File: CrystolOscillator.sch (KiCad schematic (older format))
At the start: 4 parts, among them Y501 32.768kHz, Y502 48MHz

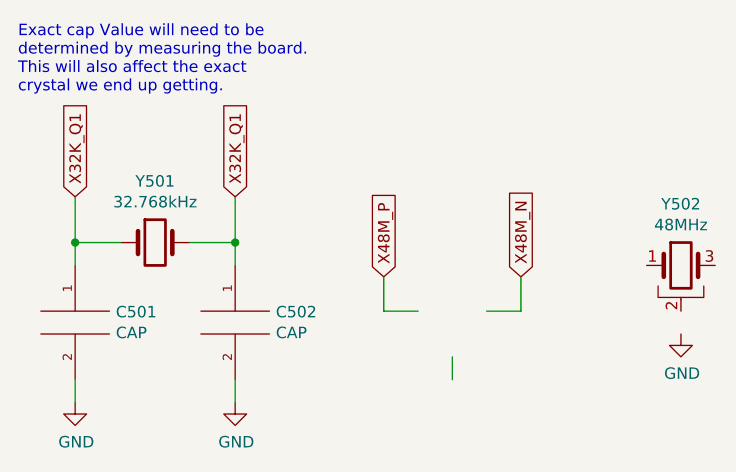
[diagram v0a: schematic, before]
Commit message: fixed the 20dBm branch and switched back to the 3 port band switcher IC
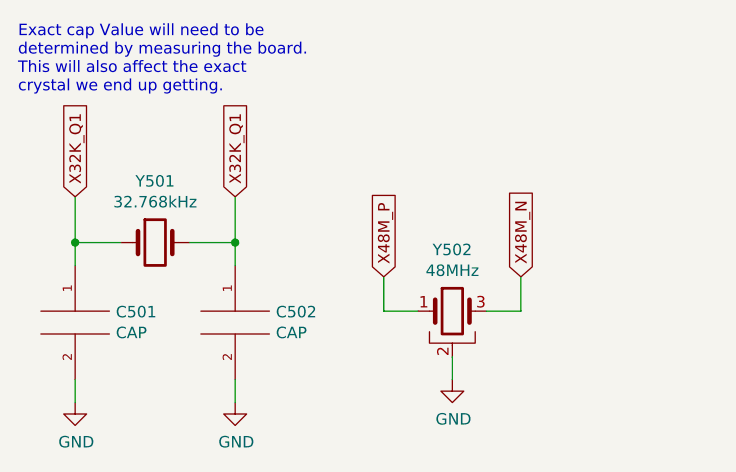
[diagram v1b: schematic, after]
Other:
- moved on the sheet: Y502
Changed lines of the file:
@@
 L Device:Crystal_GND2 Y502
 U 1 1 613841EB
-P 5000 1850
-F 0 "Y502" H 5000 2118 50  0000 C CNN
-F 1 "48MHz" H 5000 2027 50  0000 C CNN
-F 2 "Crystal:Crystal_SMD_2016-4Pin_2.0x1.6mm" H 5000 1850 50  0001 C CNN
-F 3 "https://www.mouser.com/datasheet/2/909/cx2016db_e-1316650.pdf" H 5000 1850 50  0001 C CNN
-	1    5000 1850
+P 4000 2050
+F 0 "Y502" H 4000 2318 50  0000 C CNN
+F 1 "48MHz" H 4000 2227 50  0000 C CNN
+F 2 "Crystal:Crystal_SMD_2016-4Pin_2.0x1.6mm" H 4000 2050 50  0001 C CNN
+F 3 "https://www.mouser.com/datasheet/2/909/cx2016db_e-1316650.pdf" H 4000 2050 50  0001 C CNN
+	1    4000 2050
 	1    0    0    -1
 $EndComp
@@
 L power:GND #PWR0503
 U 1 1 613863D7
-P 5000 2150
-F 0 "#PWR0503" H 5000 1900 50  0001 C CNN
-F 1 "GND" H 5005 1977 50  0000 C CNN
-F 2 "" H 5000 2150 50  0001 C CNN
-F 3 "" H 5000 2150 50  0001 C CNN
-	1    5000 2150
+P 4000 2350
+F 0 "#PWR0503" H 4000 2100 50  0001 C CNN
+F 1 "GND" H 4005 2177 50  0000 C CNN
+F 2 "" H 4000 2350 50  0001 C CNN
+F 3 "" H 4000 2350 50  0001 C CNN
+	1    4000 2350
 	1    0    0    -1
 $EndComp
